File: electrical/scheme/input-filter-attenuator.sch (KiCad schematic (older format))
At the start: 13 parts, among them U4 AD8672

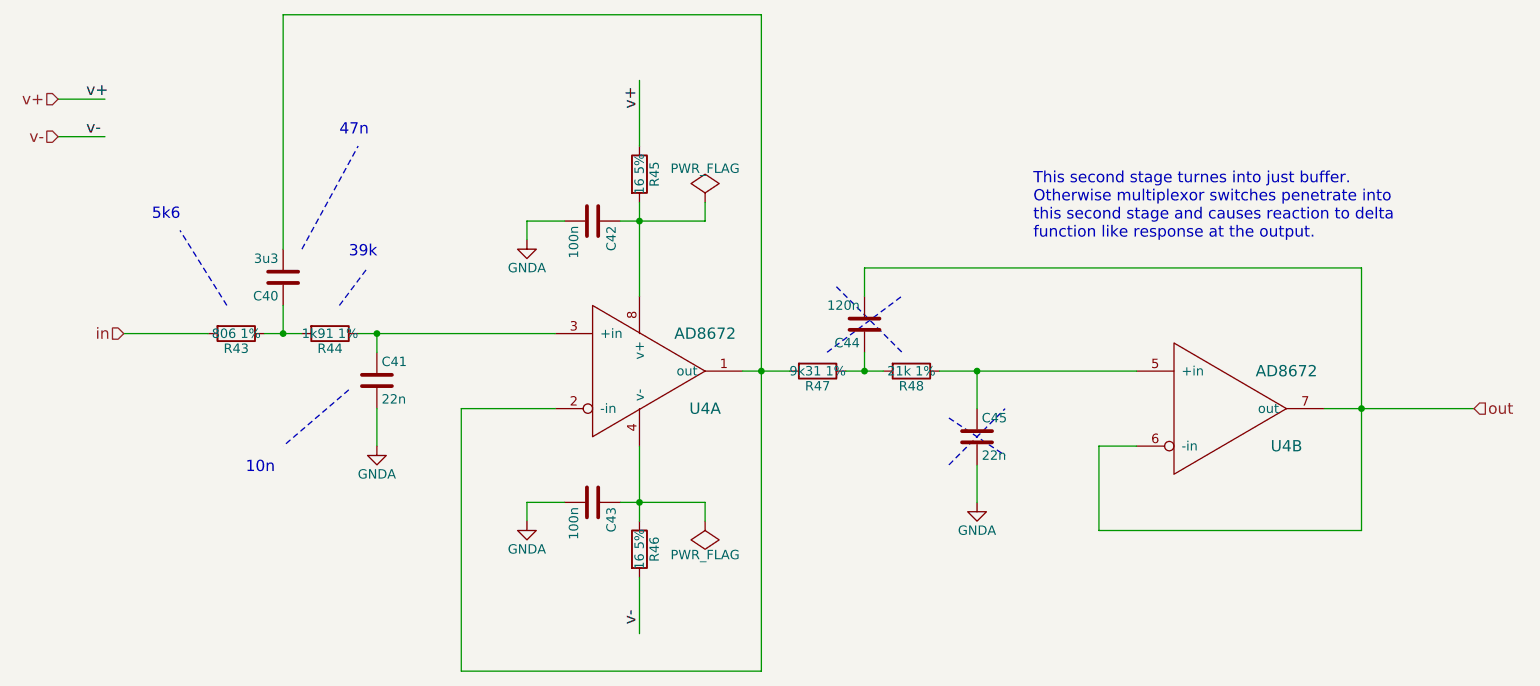
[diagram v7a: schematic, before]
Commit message: Added some improvements. But if just 1kOhm resistor added in between filter and multiplexer it solves switch spike back propagation into filter. And it eliminates mutual signal interference.
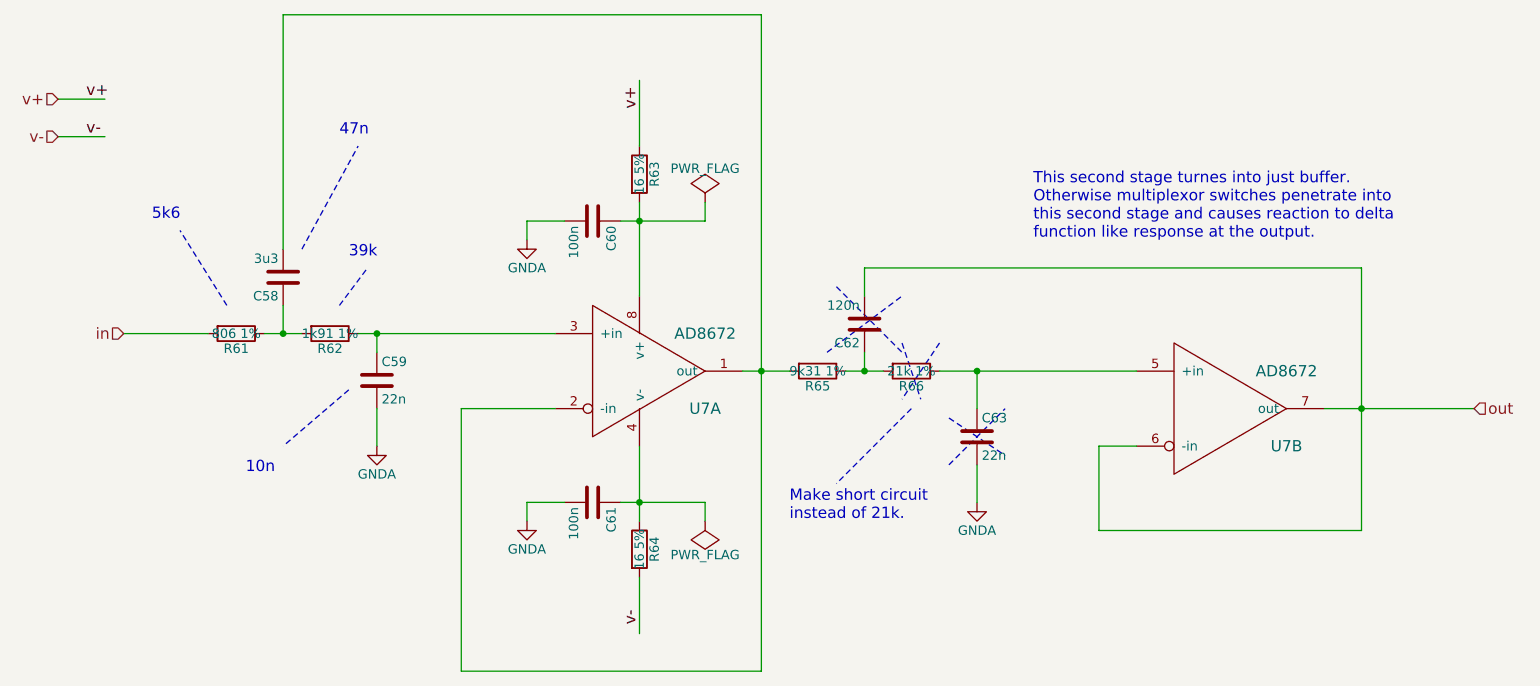
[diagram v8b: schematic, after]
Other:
- note added: "Make short circuit \ninstead of 21k."
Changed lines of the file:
@@
 $Descr A4 11693 8268
 encoding utf-8
-Sheet 2 7
+Sheet 5 7
 Title ""
 Date ""
@@
 AR Path="/55AAFE8D/55A8C542" Ref="U6"  Part="1"
 AR Path="/55AAFE9C/55A8C542" Ref="U7"  Part="1"
-F 0 "U4" H 5600 3650 60  0000 C CNN
+F 0 "U7" H 5600 3650 60  0000 C CNN
 F 1 "AD8672" H 5600 4050 60  0000 C CNN
 F 2 "Housings_SOIC:SOIC-8_3.9x4.9mm_Pitch1.27mm" H 5300 3850 60  0001 C CNN
@@
 AR Path="/55AAFE8D/55A8C549" Ref="U6"  Part="2"
 AR Path="/55AAFE9C/55A8C549" Ref="U7"  Part="2"
-F 0 "U4" H 8700 3850 60  0000 C CNN
+F 0 "U7" H 8700 3850 60  0000 C CNN
 F 1 "AD8672" H 8700 4250 60  0000 C CNN
 F 2 "Housings_SOIC:SOIC-8_3.9x4.9mm_Pitch1.27mm" H 8400 4050 60  0001 C CNN
@@
 AR Path="/55AAFE8D/55A8C74B" Ref="R57"  Part="1"
 AR Path="/55AAFE9C/55A8C74B" Ref="R63"  Part="1"
-F 0 "R45" V 5330 2800 50  0000 C CNN
+F 0 "R63" V 5330 2800 50  0000 C CNN
 F 1 "16 5%" V 5250 2800 50  0000 C CNN
 F 2 "Resistors_SMD:R_0805_HandSoldering" V 5180 2800 30  0001 C CNN
@@
 AR Path="/55AAFE8D/55A8C77D" Ref="C54"  Part="1"
 AR Path="/55AAFE9C/55A8C77D" Ref="C60"  Part="1"
-F 0 "C42" H 5025 3150 50  0000 L CNN
+F 0 "C60" H 5025 3150 50  0000 L CNN
 F 1 "100n" H 5025 2950 50  0000 L CNN
 F 2 "Capacitors_SMD:C_0805_HandSoldering" H 5038 2900 30  0001 C CNN
@@
 AR Path="/55AAFE8D/55A8C85F" Ref="#PWR0145"  Part="1"
 AR Path="/55AAFE9C/55A8C85F" Ref="#PWR0151"  Part="1"
-F 0 "#PWR0133" H 4650 2900 50  0001 C CNN
+F 0 "#PWR0151" H 4650 2900 50  0001 C CNN
 F 1 "GNDA" H 4650 3000 50  0000 C CNN
 F 2 "" H 4650 3150 60  0000 C CNN
@@
 AR Path="/55AAFE8D/55A8C8A7" Ref="R58"  Part="1"
 AR Path="/55AAFE9C/55A8C8A7" Ref="R64"  Part="1"
-F 0 "R46" V 5330 4800 50  0000 C CNN
+F 0 "R64" V 5330 4800 50  0000 C CNN
 F 1 "16 5%" V 5250 4800 50  0000 C CNN
 F 2 "Resistors_SMD:R_0805_HandSoldering" V 5180 4800 30  0001 C CNN
@@
 AR Path="/55AAFE8D/55A8CC9D" Ref="C55"  Part="1"
 AR Path="/55AAFE9C/55A8CC9D" Ref="C61"  Part="1"
-F 0 "C43" H 5025 4650 50  0000 L CNN
+F 0 "C61" H 5025 4650 50  0000 L CNN
 F 1 "100n" H 5025 4450 50  0000 L CNN
 F 2 "Capacitors_SMD:C_0805_HandSoldering" H 5038 4400 30  0001 C CNN
@@
 AR Path="/55AAFE8D/55A8CCA5" Ref="#PWR0146"  Part="1"
 AR Path="/55AAFE9C/55A8CCA5" Ref="#PWR0152"  Part="1"
-F 0 "#PWR0134" H 4650 4400 50  0001 C CNN
+F 0 "#PWR0152" H 4650 4400 50  0001 C CNN
 F 1 "GNDA" H 4650 4500 50  0000 C CNN
 F 2 "" H 4650 4650 60  0000 C CNN
@@
 AR Path="/55AAFE8D/55A8D6B2" Ref="R55"  Part="1"
 AR Path="/55AAFE9C/55A8D6B2" Ref="R61"  Part="1"
-F 0 "R43" V 3180 3650 50  0000 C CNN
+F 0 "R61" V 3180 3650 50  0000 C CNN
 F 1 "806 1%" V 3100 3650 50  0000 C CNN
 F 2 "Resistors_SMD:R_0805_HandSoldering" V 3030 3650 30  0001 C CNN
@@
 AR Path="/55AAFE8D/55A8D707" Ref="R56"  Part="1"
 AR Path="/55AAFE9C/55A8D707" Ref="R62"  Part="1"
-F 0 "R44" V 3680 3650 50  0000 C CNN
+F 0 "R62" V 3680 3650 50  0000 C CNN
 F 1 "1k91 1%" V 3600 3650 50  0000 C CNN
 F 2 "Resistors_SMD:R_0805_HandSoldering" V 3530 3650 30  0001 C CNN
@@
 AR Path="/55AAFE8D/55A8D733" Ref="C53"  Part="1"
 AR Path="/55AAFE9C/55A8D733" Ref="C59"  Part="1"
-F 0 "C41" H 3875 4000 50  0000 L CNN
+F 0 "C59" H 3875 4000 50  0000 L CNN
 F 1 "22n" H 3875 3800 50  0000 L CNN
 F 2 "Capacitors_SMD:C_0805_HandSoldering" H 3888 3750 30  0001 C CNN
@@
 AR Path="/55AAFE8D/55A8D76D" Ref="C52"  Part="1"
 AR Path="/55AAFE9C/55A8D76D" Ref="C58"  Part="1"
-F 0 "C40" H 3375 3450 50  0000 L CNN
+F 0 "C58" H 3375 3450 50  0000 L CNN
 F 1 "3u3" H 3375 3250 50  0000 L CNN
 F 2 "Capacitors_SMD:C_0805_HandSoldering" H 3388 3200 30  0001 C CNN
@@
 AR Path="/55AAFE8D/55A8D8D4" Ref="R59"  Part="1"
 AR Path="/55AAFE9C/55A8D8D4" Ref="R65"  Part="1"
-F 0 "R47" V 6280 3850 50  0000 C CNN
+F 0 "R65" V 6280 3850 50  0000 C CNN
 F 1 "9k31 1%" V 6200 3850 50  0000 C CNN
 F 2 "Resistors_SMD:R_0805_HandSoldering" V 6130 3850 30  0001 C CNN
@@
 AR Path="/55AAFE8D/55A8DA7D" Ref="R60"  Part="1"
 AR Path="/55AAFE9C/55A8DA7D" Ref="R66"  Part="1"
-F 0 "R48" V 6780 3850 50  0000 C CNN
+F 0 "R66" V 6780 3850 50  0000 C CNN
 F 1 "21k 1%" V 6700 3850 50  0000 C CNN
 F 2 "Resistors_SMD:R_0805_HandSoldering" V 6630 3850 30  0001 C CNN
@@
 AR Path="/55AAFE8D/55A8DD2D" Ref="C56"  Part="1"
 AR Path="/55AAFE9C/55A8DD2D" Ref="C62"  Part="1"
-F 0 "C44" H 6475 3700 50  0000 L CNN
+F 0 "C62" H 6475 3700 50  0000 L CNN
 F 1 "120n" H 6475 3500 50  0000 L CNN
 F 2 "Capacitors_SMD:C_0805_HandSoldering" H 6488 3450 30  0001 C CNN
@@
 AR Path="/55AAFE8D/55A8DF47" Ref="C57"  Part="1"
 AR Path="/55AAFE9C/55A8DF47" Ref="C63"  Part="1"
-F 0 "C45" H 7075 4300 50  0000 L CNN
+F 0 "C63" H 7075 4300 50  0000 L CNN
 F 1 "22n" H 7075 4100 50  0000 L CNN
 F 2 "Capacitors_SMD:C_0805_HandSoldering" H 7088 4050 30  0001 C CNN
@@
 AR Path="/55AAFE8D/55A8F5C0" Ref="#PWR0147"  Part="1"
 AR Path="/55AAFE9C/55A8F5C0" Ref="#PWR0153"  Part="1"
-F 0 "#PWR0135" H 7050 4300 50  0001 C CNN
+F 0 "#PWR0153" H 7050 4300 50  0001 C CNN
 F 1 "GNDA" H 7050 4400 50  0000 C CNN
 F 2 "" H 7050 4550 60  0000 C CNN
@@
 AR Path="/55AAFE8D/55A8F5EF" Ref="#PWR0148"  Part="1"
 AR Path="/55AAFE9C/55A8F5EF" Ref="#PWR0154"  Part="1"
-F 0 "#PWR0136" H 3850 4000 50  0001 C CNN
+F 0 "#PWR0154" H 3850 4000 50  0001 C CNN
 F 1 "GNDA" H 3850 4100 50  0000 C CNN
 F 2 "" H 3850 4250 60  0000 C CNN
@@
 AR Path="/55AAFE8D/55BB3EFD" Ref="#FLG0149"  Part="1"
 AR Path="/55AAFE9C/55BB3EFD" Ref="#FLG0155"  Part="1"
-F 0 "#FLG0137" H 5600 3045 50  0001 C CNN
+F 0 "#FLG0155" H 5600 3045 50  0001 C CNN
 F 1 "PWR_FLAG" H 5600 3130 50  0000 C CNN
 F 2 "" H 5600 2950 60  0000 C CNN
@@
 AR Path="/55A8BFF5/55BB3F68" Ref="#FLG0138"  Part="1"
 AR Path="/55AAFE9C/55BB3F68" Ref="#FLG0156"  Part="1"
-F 0 "#FLG0138" H 5600 4745 50  0001 C CNN
+F 0 "#FLG0156" H 5600 4745 50  0001 C CNN
 F 1 "PWR_FLAG" H 5600 4830 50  0000 C CNN
 F 2 "" H 5600 4650 60  0000 C CNN
@@
 Text Notes 7350 3150 0    60   ~ 0
 This second stage turnes into just buffer.\nOtherwise multiplexor switches penetrate into \nthis second stage and causes reaction to delta \nfunction like response at the output.
+Wire Notes Line
+	6850 3700 6650 4000
+Wire Notes Line
+	6650 3700 6750 4000
+Wire Notes Line
+	6700 4050 6300 4450
+Text Notes 6050 4650 0    60   ~ 0
+Make short circuit \ninstead of 21k.
 $EndSCHEMATC
